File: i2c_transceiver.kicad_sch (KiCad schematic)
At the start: 6 parts, among them U2 PCA9306DP

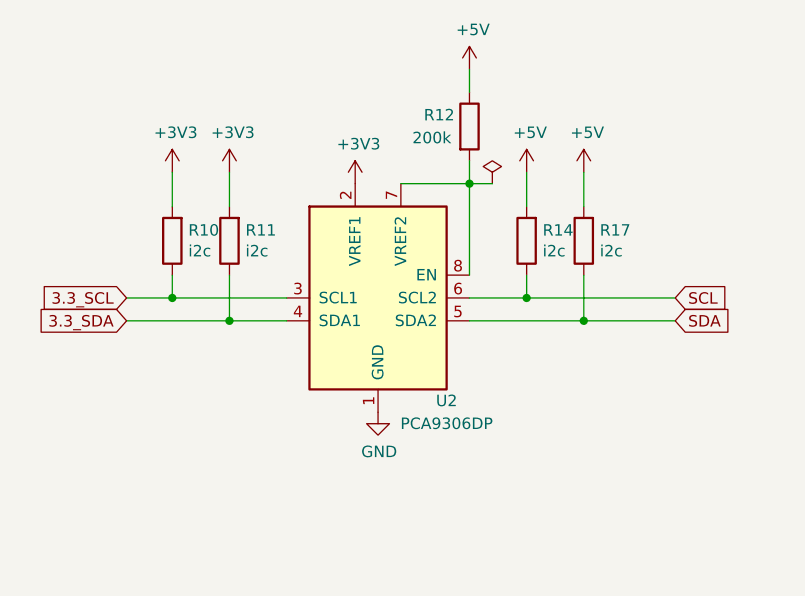
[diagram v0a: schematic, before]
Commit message: Update placement, Gerade device 3d model
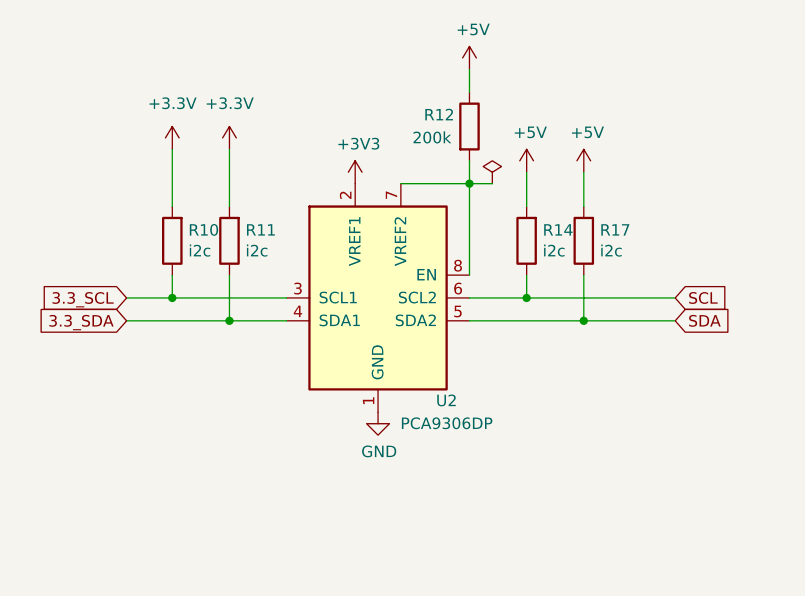
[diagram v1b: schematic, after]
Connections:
- net +3V3: no longer R10.2, R11.2
- new net +3.3V: R10.2, R11.2
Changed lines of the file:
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@@
     (stroke (width 0) (type default))
   )
-  (wire (pts (xy 132.08 76.2) (xy 132.08 80.01))
-    (stroke (width 0) (type default))
-  )
-  (wire (pts (xy 125.73 76.2) (xy 125.73 80.01))
+  (wire (pts (xy 132.08 73.66) (xy 132.08 80.01))
+    (stroke (width 0) (type default))
+  )
+  (wire (pts (xy 125.73 73.66) (xy 125.73 80.01))
     (stroke (width 0) (type default))
   )
@@
     )
   )
-  (symbol (lib_id "power:+3V3") (at 125.73 76.2 0) (unit 1)
-    (in_bom yes) (on_board yes) (dnp no)
-    (property "Reference" "#PWR025" (at 125.73 80.01 0)
-      (effects (font (size 1.27 1.27)) hide)
-    )
-    (property "Value" "+3V3" (at 126.111 71.8058 0)
-      (effects (font (size 1.27 1.27)))
-    )
-    (property "Footprint" "" (at 125.73 76.2 0)
-      (effects (font (size 1.27 1.27)) hide)
-    )
-    (property "Datasheet" "" (at 125.73 76.2 0)
-      (effects (font (size 1.27 1.27)) hide)
-    )
-    (pin "1")
-    (instances
-      (project "LTP305_ESP32_CLOCK"
-        (path "/c007e288-8439-49d9-bbdf-49724c34958c"
-          (reference "#PWR025") (unit 1)
-        )
-      )
-      (project "ltp_kikad"
-        (path "/eed35b77-cbf9-4596-9b17-2558f81058ba/2fb8f433-d537-4253-8cc8-f6d42368ed9e"
-          (reference "#PWR068") (unit 1)
-        )
-      )
-    )
-  )
   (symbol (lib_id "Device:R") (at 132.08 83.82 180) (unit 1)
     (in_bom yes) (on_board yes) (dnp no)
@@
     )
   )
-  (symbol (lib_id "power:+3V3") (at 132.08 76.2 0) (unit 1)
-    (in_bom yes) (on_board yes) (dnp no)
-    (property "Reference" "#PWR027" (at 132.08 80.01 0)
-      (effects (font (size 1.27 1.27)) hide)
-    )
-    (property "Value" "+3V3" (at 132.461 71.8058 0)
-      (effects (font (size 1.27 1.27)))
-    )
-    (property "Footprint" "" (at 132.08 76.2 0)
-      (effects (font (size 1.27 1.27)) hide)
-    )
-    (property "Datasheet" "" (at 132.08 76.2 0)
-      (effects (font (size 1.27 1.27)) hide)
-    )
-    (pin "1")
-    (instances
-      (project "LTP305_ESP32_CLOCK"
-        (path "/c007e288-8439-49d9-bbdf-49724c34958c"
-          (reference "#PWR027") (unit 1)
-        )
-      )
-      (project "ltp_kikad"
-        (path "/eed35b77-cbf9-4596-9b17-2558f81058ba/2fb8f433-d537-4253-8cc8-f6d42368ed9e"
-          (reference "#PWR069") (unit 1)
+  (symbol (lib_id "power:+3.3V") (at 132.08 73.66 0) (unit 1)
+    (in_bom yes) (on_board yes) (dnp no) (fields_autoplaced)
+    (property "Reference" "#PWR045" (at 132.08 77.47 0)
+      (effects (font (size 1.27 1.27)) hide)
+    )
+    (property "Value" "+3.3V" (at 132.08 68.58 0)
+      (effects (font (size 1.27 1.27)))
+    )
+    (property "Footprint" "" (at 132.08 73.66 0)
+      (effects (font (size 1.27 1.27)) hide)
+    )
+    (property "Datasheet" "" (at 132.08 73.66 0)
+      (effects (font (size 1.27 1.27)) hide)
+    )
+    (pin "1")
+    (instances
+      (project "ltp_kikad"
+        (path "/eed35b77-cbf9-4596-9b17-2558f81058ba/d18f2354-5f56-48bf-919b-3fdf8c87b820"
+          (reference "#PWR045") (unit 1)
+        )
+        (path "/eed35b77-cbf9-4596-9b17-2558f81058ba"
+          (reference "#PWR058") (unit 1)
+        )
+        (path "/eed35b77-cbf9-4596-9b17-2558f81058ba/2fb8f433-d537-4253-8cc8-f6d42368ed9e"
+          (reference "#PWR075") (unit 1)
         )
       )
@@
         )
       )
+    )
+  )
+  (symbol (lib_id "power:+3.3V") (at 125.73 73.66 0) (unit 1)
+    (in_bom yes) (on_board yes) (dnp no) (fields_autoplaced)
+    (property "Reference" "#PWR045" (at 125.73 77.47 0)
+      (effects (font (size 1.27 1.27)) hide)
+    )
+    (property "Value" "+3.3V" (at 125.73 68.58 0)
+      (effects (font (size 1.27 1.27)))
+    )
+    (property "Footprint" "" (at 125.73 73.66 0)
+      (effects (font (size 1.27 1.27)) hide)
+    )
+    (property "Datasheet" "" (at 125.73 73.66 0)
+      (effects (font (size 1.27 1.27)) hide)
+    )
+    (pin "1")
+    (instances
+      (project "ltp_kikad"
+        (path "/eed35b77-cbf9-4596-9b17-2558f81058ba/d18f2354-5f56-48bf-919b-3fdf8c87b820"
+          (reference "#PWR045") (unit 1)
+        )
+        (path "/eed35b77-cbf9-4596-9b17-2558f81058ba"
+          (reference "#PWR058") (unit 1)
+        )
+        (path "/eed35b77-cbf9-4596-9b17-2558f81058ba/2fb8f433-d537-4253-8cc8-f6d42368ed9e"
+          (reference "#PWR068") (unit 1)
+        )
+      )

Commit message: Version 0.05
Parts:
- R14, R17: footprint Resistor_SMD:R_0805_2012Metric_Pad1.20x1.40mm_HandSolder -> Resistor_SMD:R_0603_1608Metric
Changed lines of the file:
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@@
       (effects (font (size 1.27 1.27)) (justify right))
     )
-    (property "Footprint" "Resistor_SMD:R_0805_2012Metric_Pad1.20x1.40mm_HandSolder" (at 166.878 83.82 90)
+    (property "Footprint" "Resistor_SMD:R_0603_1608Metric" (at 166.878 83.82 90)
       (effects (font (size 1.27 1.27)) hide)
     )
@@
       (effects (font (size 1.27 1.27)) (justify right))
     )
-    (property "Footprint" "Resistor_SMD:R_0805_2012Metric_Pad1.20x1.40mm_HandSolder" (at 173.228 83.82 90)
+    (property "Footprint" "Resistor_SMD:R_0603_1608Metric" (at 173.228 83.82 90)
       (effects (font (size 1.27 1.27)) hide)
     )

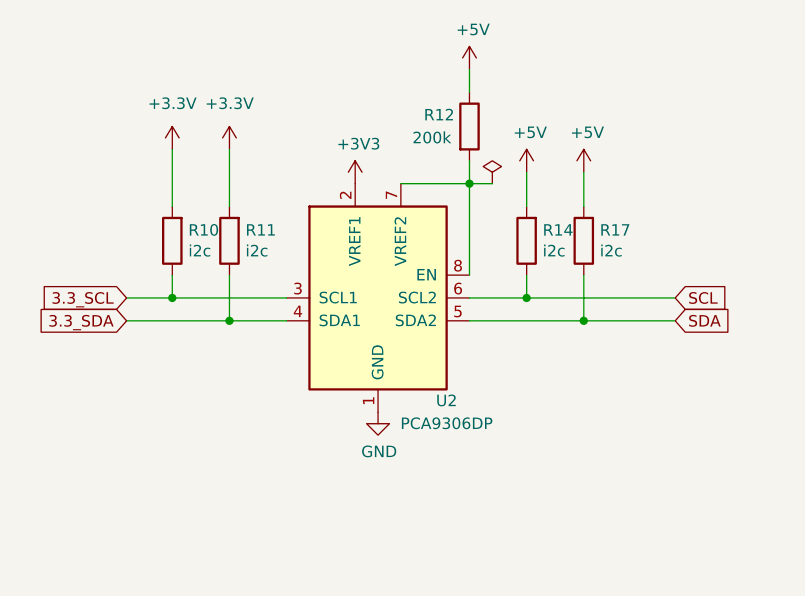
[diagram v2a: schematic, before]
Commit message: Add testpoints
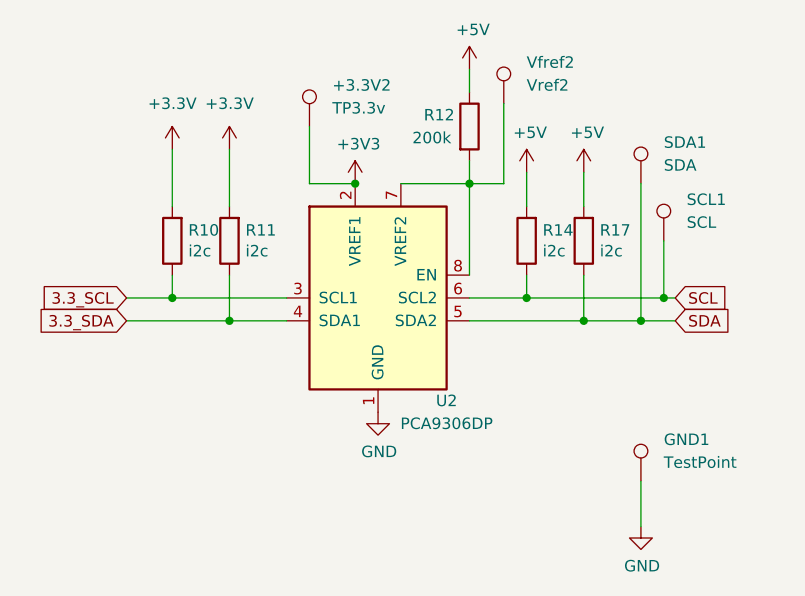
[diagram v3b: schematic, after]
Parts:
- added +3.3V2: TP3.3v, TestPoint:TestPoint_Pad_D1.0mm, symbol Connector:TestPoint
- added GND1: TestPoint, TestPoint:TestPoint_Pad_D1.0mm, symbol Connector:TestPoint
- added SCL1: SCL, TestPoint:TestPoint_Pad_D1.0mm, symbol Connector:TestPoint
- added SDA1: SDA, TestPoint:TestPoint_Pad_D1.0mm, symbol Connector:TestPoint
- added Vfref2: Vref2, TestPoint:TestPoint_Pad_D1.0mm, symbol Connector:TestPoint
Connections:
- net +3V3: now also +3.3V2.1
- net GND: now also GND1.1
- net SCL: now also SCL1.1
- net SDA: now also SDA1.1
- net at R12.2, U2.7 (VREF2), U2.8 (EN): now also Vfref2.1
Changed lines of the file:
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@@
   (junction (at 125.73 90.17) (diameter 0) (color 0 0 0 0)
   )
+  (junction (at 180.34 90.17) (diameter 0) (color 0 0 0 0)
+  )
+  (junction (at 146.05 77.47) (diameter 0) (color 0 0 0 0)
+  )
   (junction (at 165.1 90.17) (diameter 0) (color 0 0 0 0)
   )
@@
   (junction (at 132.08 92.71) (diameter 0) (color 0 0 0 0)
   )
+  (junction (at 177.8 92.71) (diameter 0) (color 0 0 0 0)
+  )
   (wire (pts (xy 158.75 90.17) (xy 165.1 90.17))
     (stroke (width 0) (type default))
@@
     (stroke (width 0) (type default))
   )
-  (wire (pts (xy 171.45 92.71) (xy 181.61 92.71))
+  (wire (pts (xy 171.45 92.71) (xy 177.8 92.71))
     (stroke (width 0) (type default))
   )
@@
     (stroke (width 0) (type default))
   )
-  (wire (pts (xy 161.29 77.47) (xy 158.75 77.47))
+  (wire (pts (xy 140.97 71.12) (xy 140.97 77.47))
+    (stroke (width 0) (type default))
+  )
+  (wire (pts (xy 158.75 77.47) (xy 162.56 77.47))
     (stroke (width 0) (type default))
   )
@@
     (stroke (width 0) (type default))
   )
+  (wire (pts (xy 177.8 110.49) (xy 177.8 115.57))
+    (stroke (width 0) (type default))
+  )
+  (wire (pts (xy 140.97 77.47) (xy 146.05 77.47))
+    (stroke (width 0) (type default))
+  )
   (wire (pts (xy 125.73 87.63) (xy 125.73 90.17))
     (stroke (width 0) (type default))
@@
     (stroke (width 0) (type default))
   )
-  (wire (pts (xy 165.1 90.17) (xy 181.61 90.17))
+  (wire (pts (xy 165.1 90.17) (xy 180.34 90.17))
     (stroke (width 0) (type default))
   )
@@
     (stroke (width 0) (type default))
   )
+  (wire (pts (xy 177.8 77.47) (xy 177.8 92.71))
+    (stroke (width 0) (type default))
+  )
+  (wire (pts (xy 180.34 83.82) (xy 180.34 90.17))
+    (stroke (width 0) (type default))
+  )
+  (wire (pts (xy 177.8 92.71) (xy 181.61 92.71))
+    (stroke (width 0) (type default))
+  )
   (wire (pts (xy 120.65 92.71) (xy 132.08 92.71))
     (stroke (width 0) (type default))
   )
+  (wire (pts (xy 162.56 68.58) (xy 162.56 77.47))
+    (stroke (width 0) (type default))
+  )
   (wire (pts (xy 132.08 87.63) (xy 132.08 92.71))
+    (stroke (width 0) (type default))
+  )
+  (wire (pts (xy 180.34 90.17) (xy 181.61 90.17))
     (stroke (width 0) (type default))
   )
@@
     )
   )
+  (symbol (lib_id "Connector:TestPoint") (at 162.56 68.58 0) (unit 1)
+    (in_bom yes) (on_board yes) (dnp no) (fields_autoplaced)
+    (property "Reference" "Vfref2" (at 165.1 64.008 0)
+      (effects (font (size 1.27 1.27)) (justify left))
+    )
+    (property "Value" "Vref2" (at 165.1 66.548 0)
+      (effects (font (size 1.27 1.27)) (justify left))
+    )
+    (property "Footprint" "TestPoint:TestPoint_Pad_D1.0mm" (at 167.64 68.58 0)
+      (effects (font (size 1.27 1.27)) hide)
+    )
+    (property "Datasheet" "~" (at 167.64 68.58 0)
+      (effects (font (size 1.27 1.27)) hide)
+    )
+    (pin "1")
+    (instances
+      (project "ltp_kikad"
+        (path "/eed35b77-cbf9-4596-9b17-2558f81058ba/2fb8f433-d537-4253-8cc8-f6d42368ed9e"
+          (reference "Vfref2") (unit 1)
+        )
+      )
+    )
+  )
   (symbol (lib_id "Device:R") (at 165.1 83.82 180) (unit 1)
     (in_bom yes) (on_board yes) (dnp no)
@@
     )
   )
+  (symbol (lib_id "power:GND") (at 177.8 115.57 0) (unit 1)
+    (in_bom yes) (on_board yes) (dnp no)
+    (property "Reference" "#PWR029" (at 177.8 121.92 0)
+      (effects (font (size 1.27 1.27)) hide)
+    )
+    (property "Value" "GND" (at 177.927 119.9642 0)
+      (effects (font (size 1.27 1.27)))
+    )
+    (property "Footprint" "" (at 177.8 115.57 0)
+      (effects (font (size 1.27 1.27)) hide)
+    )
+    (property "Datasheet" "" (at 177.8 115.57 0)
+      (effects (font (size 1.27 1.27)) hide)
+    )
+    (pin "1")
+    (instances
+      (project "LTP305_ESP32_CLOCK"
+        (path "/c007e288-8439-49d9-bbdf-49724c34958c"
+          (reference "#PWR029") (unit 1)
+        )
+      )
+      (project "ltp_kikad"
+        (path "/eed35b77-cbf9-4596-9b17-2558f81058ba/2fb8f433-d537-4253-8cc8-f6d42368ed9e"
+          (reference "#PWR037") (unit 1)
+        )
+      )
+    )
+  )
+  (symbol (lib_id "Connector:TestPoint") (at 177.8 110.49 0) (unit 1)
+    (in_bom yes) (on_board yes) (dnp no) (fields_autoplaced)
+    (property "Reference" "GND1" (at 180.34 105.918 0)
+      (effects (font (size 1.27 1.27)) (justify left))
+    )
+    (property "Value" "TestPoint" (at 180.34 108.458 0)
+      (effects (font (size 1.27 1.27)) (justify left))
+    )
+    (property "Footprint" "TestPoint:TestPoint_Pad_D1.0mm" (at 182.88 110.49 0)
+      (effects (font (size 1.27 1.27)) hide)
+    )
+    (property "Datasheet" "~" (at 182.88 110.49 0)
+      (effects (font (size 1.27 1.27)) hide)
+    )
+    (pin "1")
+    (instances
+      (project "ltp_kikad"
+        (path "/eed35b77-cbf9-4596-9b17-2558f81058ba/2fb8f433-d537-4253-8cc8-f6d42368ed9e"
+          (reference "GND1") (unit 1)
+        )
+      )
+    )
+  )
   (symbol (lib_id "Device:R") (at 132.08 83.82 180) (unit 1)
     (in_bom yes) (on_board yes) (dnp no)
@@
         (path "/eed35b77-cbf9-4596-9b17-2558f81058ba/2fb8f433-d537-4253-8cc8-f6d42368ed9e"
           (reference "R17") (unit 1)
+        )
+      )
+    )
+  )
+  (symbol (lib_id "Connector:TestPoint") (at 140.97 71.12 0) (unit 1)
+    (in_bom yes) (on_board yes) (dnp no) (fields_autoplaced)
+    (property "Reference" "+3.3V2" (at 143.51 66.548 0)
+      (effects (font (size 1.27 1.27)) (justify left))
+    )
+    (property "Value" "TP3.3v" (at 143.51 69.088 0)
+      (effects (font (size 1.27 1.27)) (justify left))
+    )
+    (property "Footprint" "TestPoint:TestPoint_Pad_D1.0mm" (at 146.05 71.12 0)
+      (effects (font (size 1.27 1.27)) hide)
+    )
+    (property "Datasheet" "~" (at 146.05 71.12 0)
+      (effects (font (size 1.27 1.27)) hide)
+    )
+    (pin "1")
+    (instances
+      (project "ltp_kikad"
+        (path "/eed35b77-cbf9-4596-9b17-2558f81058ba/2fb8f433-d537-4253-8cc8-f6d42368ed9e"
+          (reference "+3.3V2") (unit 1)
         )
       )
@@
         (path "/eed35b77-cbf9-4596-9b17-2558f81058ba/2fb8f433-d537-4253-8cc8-f6d42368ed9e"
           (reference "#PWR075") (unit 1)
+        )
+      )
+    )
+  )
+  (symbol (lib_id "Connector:TestPoint") (at 180.34 83.82 0) (unit 1)
+    (in_bom yes) (on_board yes) (dnp no) (fields_autoplaced)
+    (property "Reference" "SCL1" (at 182.88 79.248 0)
+      (effects (font (size 1.27 1.27)) (justify left))
+    )
+    (property "Value" "SCL" (at 182.88 81.788 0)
+      (effects (font (size 1.27 1.27)) (justify left))
+    )
+    (property "Footprint" "TestPoint:TestPoint_Pad_D1.0mm" (at 185.42 83.82 0)
+      (effects (font (size 1.27 1.27)) hide)
+    )
+    (property "Datasheet" "~" (at 185.42 83.82 0)
+      (effects (font (size 1.27 1.27)) hide)
+    )
+    (pin "1")
+    (instances
+      (project "ltp_kikad"
+        (path "/eed35b77-cbf9-4596-9b17-2558f81058ba/2fb8f433-d537-4253-8cc8-f6d42368ed9e"
+          (reference "SCL1") (unit 1)
         )
       )
@@
     )
   )
+  (symbol (lib_id "Connector:TestPoint") (at 177.8 77.47 0) (unit 1)
+    (in_bom yes) (on_board yes) (dnp no) (fields_autoplaced)
+    (property "Reference" "SDA1" (at 180.34 72.898 0)
+      (effects (font (size 1.27 1.27)) (justify left))
+    )
+    (property "Value" "SDA" (at 180.34 75.438 0)
+      (effects (font (size 1.27 1.27)) (justify left))
+    )
+    (property "Footprint" "TestPoint:TestPoint_Pad_D1.0mm" (at 182.88 77.47 0)
+      (effects (font (size 1.27 1.27)) hide)
+    )
+    (property "Datasheet" "~" (at 182.88 77.47 0)
+      (effects (font (size 1.27 1.27)) hide)
+    )
+    (pin "1")
+    (instances
+      (project "ltp_kikad"
+        (path "/eed35b77-cbf9-4596-9b17-2558f81058ba/2fb8f433-d537-4253-8cc8-f6d42368ed9e"
+          (reference "SDA1") (unit 1)
+        )
+      )
+    )
+  )
   (symbol (lib_id "power:+3V3") (at 146.05 77.47 0) (unit 1)
     (in_bom yes) (on_board yes) (dnp no)
@@
         )
       )
-    )
-  )
-  (symbol (lib_id "power:PWR_FLAG") (at 161.29 77.47 0) (unit 1)
-    (in_bom yes) (on_board yes) (dnp no)
-    (property "Reference" "#FLG0103" (at 161.29 75.565 0)
-      (effects (font (size 1.27 1.27)) hide)
-    )
-    (property "Value" "PWR_FLAG" (at 161.29 73.0758 0)
-      (effects (font (size 1.27 1.27)) hide)
-    )
-    (property "Footprint" "" (at 161.29 77.47 0)
-      (effects (font (size 1.27 1.27)) hide)
-    )
-    (property "Datasheet" "~" (at 161.29 77.47 0)
-      (effects (font (size 1.27 1.27)) hide)
-    )
-    (pin "1")
-    (instances
-      (project "LTP305_ESP32_CLOCK"
-        (path "/c007e288-8439-49d9-bbdf-49724c34958c"
-          (reference "#FLG0103") (unit 1)
-        )
-      )
-      (project "ltp_kikad"
-        (path "/eed35b77-cbf9-4596-9b17-2558f81058ba/2fb8f433-d537-4253-8cc8-f6d42368ed9e"
-          (reference "#FLG01") (unit 1)
-        )
-      )

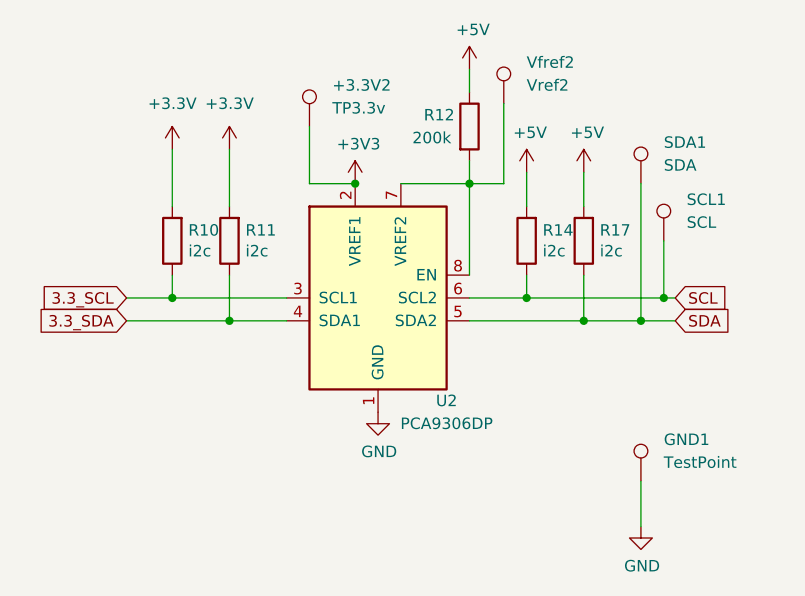
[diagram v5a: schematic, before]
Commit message: Add mcp 2517 can transceiver
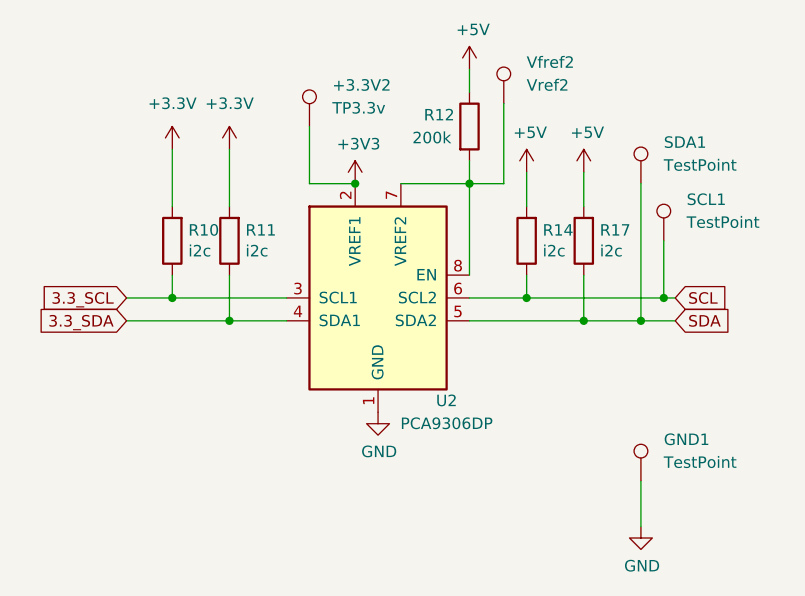
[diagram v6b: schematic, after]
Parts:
- SCL1: value SCL -> TestPoint
- SDA1: value SDA -> TestPoint
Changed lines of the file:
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@@
       (effects (font (size 1.27 1.27)) (justify left))
     )
-    (property "Value" "SCL" (at 182.88 81.788 0)
+    (property "Value" "TestPoint" (at 182.88 81.788 0)
       (effects (font (size 1.27 1.27)) (justify left))
     )
@@
       (effects (font (size 1.27 1.27)) (justify left))
     )
-    (property "Value" "SDA" (at 180.34 75.438 0)
+    (property "Value" "TestPoint" (at 180.34 75.438 0)
       (effects (font (size 1.27 1.27)) (justify left))
     )
